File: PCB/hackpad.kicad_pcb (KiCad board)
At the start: 2 copper layers, 79.5 x 100 mm, 34 parts, among them SW1 SW_Push, SW10 SW_Push, SW11 SW_Push, SW12 SW_Push, SW13 SW_Push, SW14 SW_Push, SW15 SW_Push, SW16 SW_Push, SW2 SW_Push, SW3 SW_Push, SW4 SW_Push, SW5 SW_Push, SW6 SW_Push, SW7 SW_Push, SW8 SW_Push, SW9 SW_Push, U1 XIAO-RP2040-DIP

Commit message: Final update
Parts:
- added G***: LOGO, LOGO, B.Cu at (110.5, 98.5)

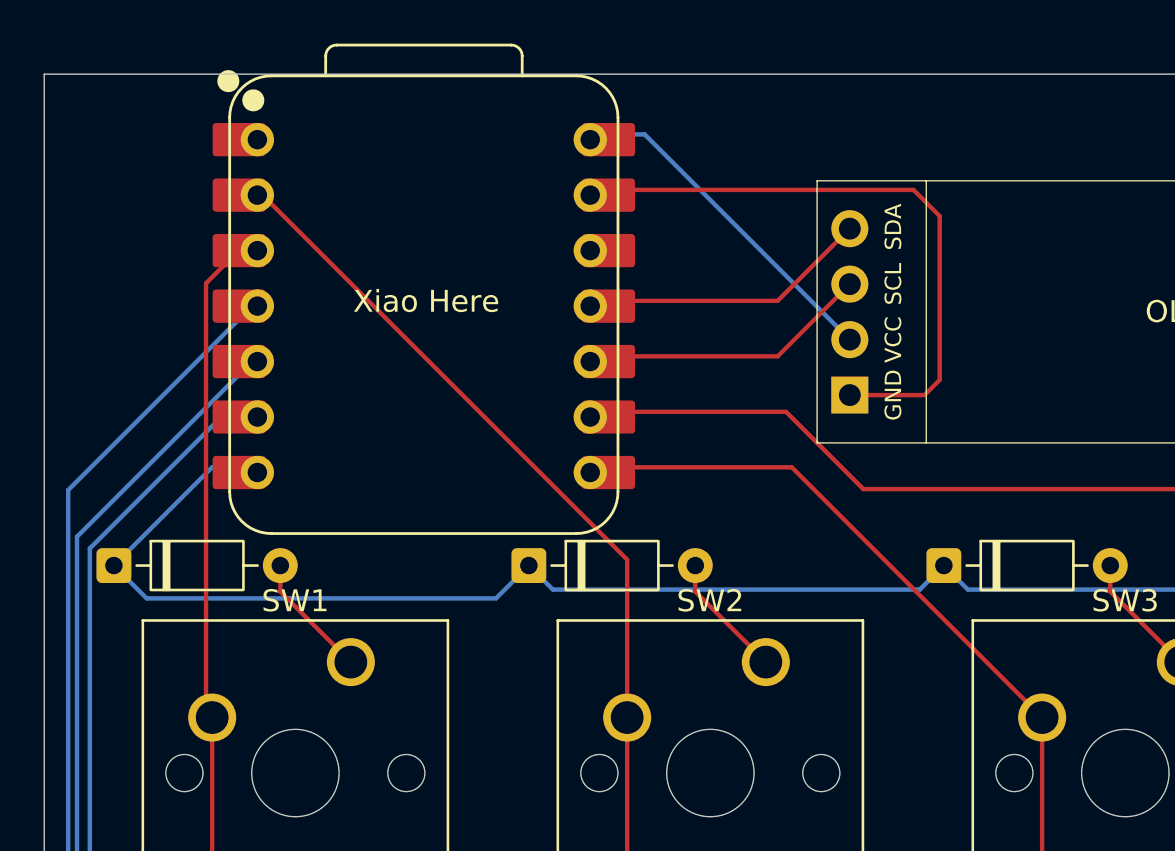
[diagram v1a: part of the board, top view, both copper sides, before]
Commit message: Fix PCB for if anyone tries to use this project for refrence
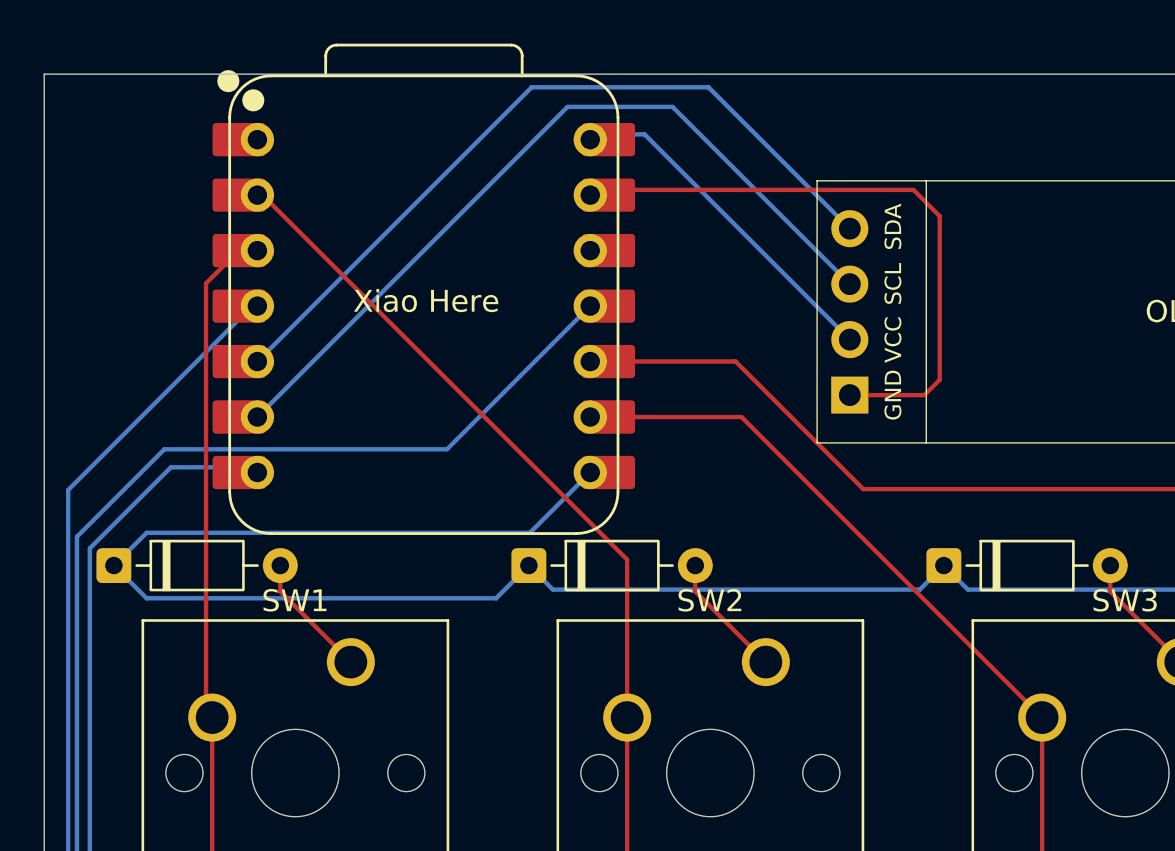
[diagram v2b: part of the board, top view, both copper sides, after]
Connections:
- U1 pad 10: Net-(U1-GPIO4/MISO) -> Column3
- U1 pad 11: Net-(U1-GPIO3/MOSI) -> Row2
- U1 pad 5: Row2 -> Net-(U1-GPIO6/SDA)
- U1 pad 6: Row1 -> Net-(U1-GPIO7/SCL)
- U1 pad 7: Row0 -> Row1
- U1 pad 8: Column2 -> Row0
- U1 pad 9: Column3 -> Column2
- U2 pad 3: Net-(U1-GPIO4/MISO) -> Net-(U1-GPIO7/SCL)
- U2 pad 4: Net-(U1-GPIO3/MOSI) -> Net-(U1-GPIO6/SDA)
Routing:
- net Net-(U1-GPIO7/SCL): track 0.00 -> 37.8 mm
- net Net-(U1-GPIO6/SDA): track 0.00 -> 35.0 mm
- net Row2: track 110.8 -> 129.3 mm
- net Net-(U1-GPIO3/MOSI): track 15.6 -> 0.00 mm
- net Row0: track 68.8 -> 84.0 mm
- net Net-(U1-GPIO4/MISO): track 13.3 -> 0.00 mm
- net Row1: track 90.2 -> 89.2 mm
- net Column3: track 102.5 -> 103.4 mm
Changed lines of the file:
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@@
 	(net 26 "unconnected-(U1-3V3-Pad12)")
 	(net 27 "+5V")
-	(net 28 "Net-(U1-GPIO4{slash}MISO)")
-	(net 29 "Net-(U1-GPIO3{slash}MOSI)")
+	(net 28 "Net-(U1-GPIO7{slash}SCL)")
+	(net 29 "Net-(U1-GPIO6{slash}SDA)")
 	(net 30 "unconnected-(U1-GPIO26{slash}ADC0{slash}A0-Pad1)")
 	(footprint "Diode_THT:D_DO-35_SOD27_P7.62mm_Horizontal"
@@
 			(layers "*.Cu" "*.Mask")
 			(remove_unused_layers no)
-			(net 28 "Net-(U1-GPIO4{slash}MISO)")
+			(net 28 "Net-(U1-GPIO7{slash}SCL)")
 			(pinfunction "SCL")
 			(pintype "input")
@@
 			(layers "*.Cu" "*.Mask")
 			(remove_unused_layers no)
-			(net 29 "Net-(U1-GPIO3{slash}MOSI)")
+			(net 29 "Net-(U1-GPIO6{slash}SDA)")
 			(pinfunction "SDA")
 			(pintype "input")
@@
 			(layers "F.Cu" "F.Mask")
 			(roundrect_rratio 0.1)
-			(net 7 "Row2")
+			(net 29 "Net-(U1-GPIO6{slash}SDA)")
 			(pinfunction "GPIO6/SDA")
 			(pintype "passive")
@@
 			(layers "*.Cu" "*.Mask")
 			(remove_unused_layers no)
-			(net 7 "Row2")
+			(net 29 "Net-(U1-GPIO6{slash}SDA)")
 			(pinfunction "GPIO6/SDA")
 			(pintype "passive")
@@
 			(layers "F.Cu" "F.Mask")
 			(roundrect_rratio 0.1)
-			(net 12 "Row1")
+			(net 28 "Net-(U1-GPIO7{slash}SCL)")
 			(pinfunction "GPIO7/SCL")
 			(pintype "passive")
@@
 			(layers "*.Cu" "*.Mask")
 			(remove_unused_layers no)
-			(net 12 "Row1")
+			(net 28 "Net-(U1-GPIO7{slash}SCL)")
 			(pinfunction "GPIO7/SCL")
 			(pintype "passive")
@@
 			(layers "F.Cu" "F.Mask")
 			(roundrect_rratio 0.1)
-			(net 16 "Row0")
+			(net 12 "Row1")
 			(pinfunction "GPIO0/TX")
 			(pintype "passive")
@@
 			(layers "*.Cu" "*.Mask")
 			(remove_unused_layers no)
-			(net 16 "Row0")
+			(net 12 "Row1")
 			(pinfunction "GPIO0/TX")
 			(pintype "passive")
@@
 			(layers "*.Cu" "*.Mask")
 			(remove_unused_layers no)
-			(net 23 "Column2")
+			(net 16 "Row0")
 			(pinfunction "GPIO1/RX")
 			(pintype "passive")
@@
 			(layers "F.Cu" "F.Mask")
 			(roundrect_rratio 0.1)
-			(net 23 "Column2")
+			(net 16 "Row0")
 			(pinfunction "GPIO1/RX")
 			(pintype "passive")
@@
 			(layers "*.Cu" "*.Mask")
 			(remove_unused_layers no)
-			(net 24 "Column3")
+			(net 23 "Column2")
 			(pinfunction "GPIO2/SCK")
 			(pintype "passive")
@@
 			(layers "F.Cu" "F.Mask")
 			(roundrect_rratio 0.1)
-			(net 24 "Column3")
+			(net 23 "Column2")
 			(pinfunction "GPIO2/SCK")
 			(pintype "passive")
@@
 			(layers "*.Cu" "*.Mask")
 			(remove_unused_layers no)
-			(net 28 "Net-(U1-GPIO4{slash}MISO)")
+			(net 24 "Column3")
 			(pinfunction "GPIO4/MISO")
 			(pintype "passive")
@@
 			(layers "F.Cu" "F.Mask")
 			(roundrect_rratio 0.1)
-			(net 28 "Net-(U1-GPIO4{slash}MISO)")
+			(net 24 "Column3")
 			(pinfunction "GPIO4/MISO")
 			(pintype "passive")
@@
 			(layers "*.Cu" "*.Mask")
 			(remove_unused_layers no)
-			(net 29 "Net-(U1-GPIO3{slash}MOSI)")
+			(net 7 "Row2")
 			(pinfunction "GPIO3/MOSI")
 			(pintype "passive")
@@
 			(layers "F.Cu" "F.Mask")
 			(roundrect_rratio 0.1)
-			(net 29 "Net-(U1-GPIO3{slash}MOSI)")
+			(net 7 "Row2")
 			(pinfunction "GPIO3/MOSI")
 			(pintype "passive")
@@
 	)
 	(segment
-		(start 80.76 55.42)
+		(start 96 52.88)
+		(end 97.58 52.88)
+		(width 0.2)
+		(layer "F.Cu")
+		(net 7)
+	)
+	(segment
+		(start 97.58 52.88)
+		(end 96.835 52.88)
+		(width 0.2)
+		(layer "F.Cu")
+		(net 7)
+	)
+	(segment
+		(start 76.503 59.677)
 		(end 72.5 63.68)
 		(width 0.2)
@@
 	)
 	(segment
+		(start 89.443 59.677)
+		(end 76.503 59.677)
+		(width 0.2)
+		(layer "B.Cu")
+		(net 7)
+	)
+	(segment
 		(start 111.589 104.101)
 		(end 112.19 103.5)
@@
 	)
 	(segment
+		(start 96 53.12)
+		(end 89.443 59.677)
+		(width 0.2)
+		(layer "B.Cu")
+		(net 7)
+	)
+	(segment
 		(start 130.69 104)
 		(end 131.19 103.5)
@@
 	)
 	(segment
-		(start 73.089 64.21484)
-		(end 73.089 82.899)
+		(start 76.80384 60.5)
+		(end 73.089 64.21484)
+		(width 0.2)
+		(layer "B.Cu")
+		(net 12)
+	)
+	(segment
+		(start 80.76 60.5)
+		(end 76.80384 60.5)
 		(width 0.2)
 		(layer "B.Cu")
@@
 	)
 	(segment
-		(start 73.089 82.899)
-		(end 74.19 84)
+		(start 73.089 64.21484)
+		(end 73.089 82.899)
 		(width 0.2)
 		(layer "B.Cu")
@@
 	)
 	(segment
+		(start 73.089 82.899)
+		(end 74.19 84)
+		(width 0.2)
+		(layer "B.Cu")
+		(net 12)
+	)
+	(segment
 		(start 111.089 85.101)
 		(end 112.19 84)
@@
 	)
 	(segment
-		(start 79.34384 57.96)
-		(end 73.089 64.21484)
-		(width 0.2)
-		(layer "B.Cu")
-		(net 12)
-	)
-	(segment
-		(start 80.76 57.96)
-		(end 79.34384 57.96)
-		(width 0.2)
-		(layer "B.Cu")
-		(net 12)
-	)
-	(segment
 		(start 100.81 104.19)
 		(end 104.04 107.42)
@@
 	)
 	(segment
-		(start 80.76 60.5)
-		(end 78.69 60.5)
+		(start 92.88 65)
+		(end 93.19 65)
 		(width 0.2)
 		(layer "B.Cu")
@@
 	)
 	(segment
-		(start 78.69 60.5)
-		(end 74.19 65)
+		(start 93.24 63.5)
+		(end 75.69 63.5)
 		(width 0.2)
 		(layer "B.Cu")
@@
 	)
 	(segment
-		(start 92.88 65)
-		(end 93.19 65)
+		(start 93.19 65)
+		(end 91.69 66.5)
 		(width 0.2)
 		(layer "B.Cu")
@@
 	)
 	(segment
-		(start 93.19 65)
-		(end 91.69 66.5)
+		(start 96 60.74)
+		(end 93.24 63.5)
+		(width 0.2)
+		(layer "B.Cu")
+		(net 16)
+	)
+	(segment
+		(start 75.69 63.5)
+		(end 74.19 65)
 		(width 0.2)
 		(layer "B.Cu")
@@
 	)
 	(segment
-		(start 96 60.5)
-		(end 105.23 60.5)
+		(start 116.69 90.96)
+		(end 116.69 109.96)
 		(width 0.2)
 		(layer "F.Cu")
@@
 	)
 	(segment
-		(start 116.69 90.96)
-		(end 116.69 109.96)
+		(start 96.835 58.2)
+		(end 102.93 58.2)
 		(width 0.2)
 		(layer "F.Cu")
@@
 	)
 	(segment
-		(start 105.23 60.5)
+		(start 102.93 58.2)
 		(end 116.69 71.96)
 		(width 0.2)
@@
 	)
 	(segment
-		(start 104.96 57.96)
+		(start 102.66 55.66)
 		(end 108.5 61.5)
 		(width 0.2)
@@
 	)
 	(segment
-		(start 108.5 61.5)
-		(end 125.23 61.5)
+		(start 96 55.66)
+		(end 102.66 55.66)
 		(width 0.2)
 		(layer "F.Cu")
@@
 	)
 	(segment
-		(start 96 57.96)
-		(end 104.96 57.96)
+		(start 108.5 61.5)
+		(end 125.23 61.5)
 		(width 0.2)
 		(layer "F.Cu")
@@
 	)
 	(segment
+		(start 80.76 58.2)
+		(end 94.96 44)
+		(width 0.2)
+		(layer "B.Cu")
+		(net 28)
+	)
+	(segment
 		(start 107.885 52.115)
-		(end 104.58 55.42)
+		(end 99.77 44)
 		(width 0.2)
-		(layer "F.Cu")
+		(layer "B.Cu")
 		(net 28)
 	)
 	(segment
-		(start 104.58 55.42)
-		(end 96 55.42)
+		(start 99.77 44)
+		(end 94.96 44)
 		(width 0.2)
-		(layer "F.Cu")
+		(layer "B.Cu")
 		(net 28)
 	)
 	(segment
-		(start 104.58 52.88)
-		(end 96 52.88)
+		(start 80.76 57.96)
+		(end 79.34384 57.96)
 		(width 0.2)
-		(layer "F.Cu")
-		(net 29)
+		(layer "B.Cu")
+		(net 28)
 	)
 	(segment
-		(start 107.885 49.575)
-		(end 104.58 52.88)
+		(start 101.411 43.101)
+		(end 107.885 49.575)
 		(width 0.2)
-		(layer "F.Cu")
+		(layer "B.Cu")
 		(net 29)
 	)
 	(segment
-		(start 96 52.88)
-		(end 97.58 52.88)
+		(start 80.76 55.66)
+		(end 93.319 43.101)
 		(width 0.2)
-		(layer "F.Cu")
+		(layer "B.Cu")
 		(net 29)
 	)
 	(segment
-		(start 97.58 52.88)
-		(end 96.835 52.88)
+		(start 93.319 43.101)
+		(end 101.411 43.101)
 		(width 0.2)
-		(layer "F.Cu")
+		(layer "B.Cu")
 		(net 29)
 	)
